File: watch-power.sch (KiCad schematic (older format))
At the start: 67 parts, among them IC1 TPS63030, IC2 MMBT2222ALT1G, IC3 BQ24230, IC4 DRV2603RUNR, IC5 LC709203F, J1 47346-0001, J2 1-1734592-4, J3 Battery, M1 Vibramotor, U1 nRF52832-QFxx, U2 APDS9960, U3 ST7735

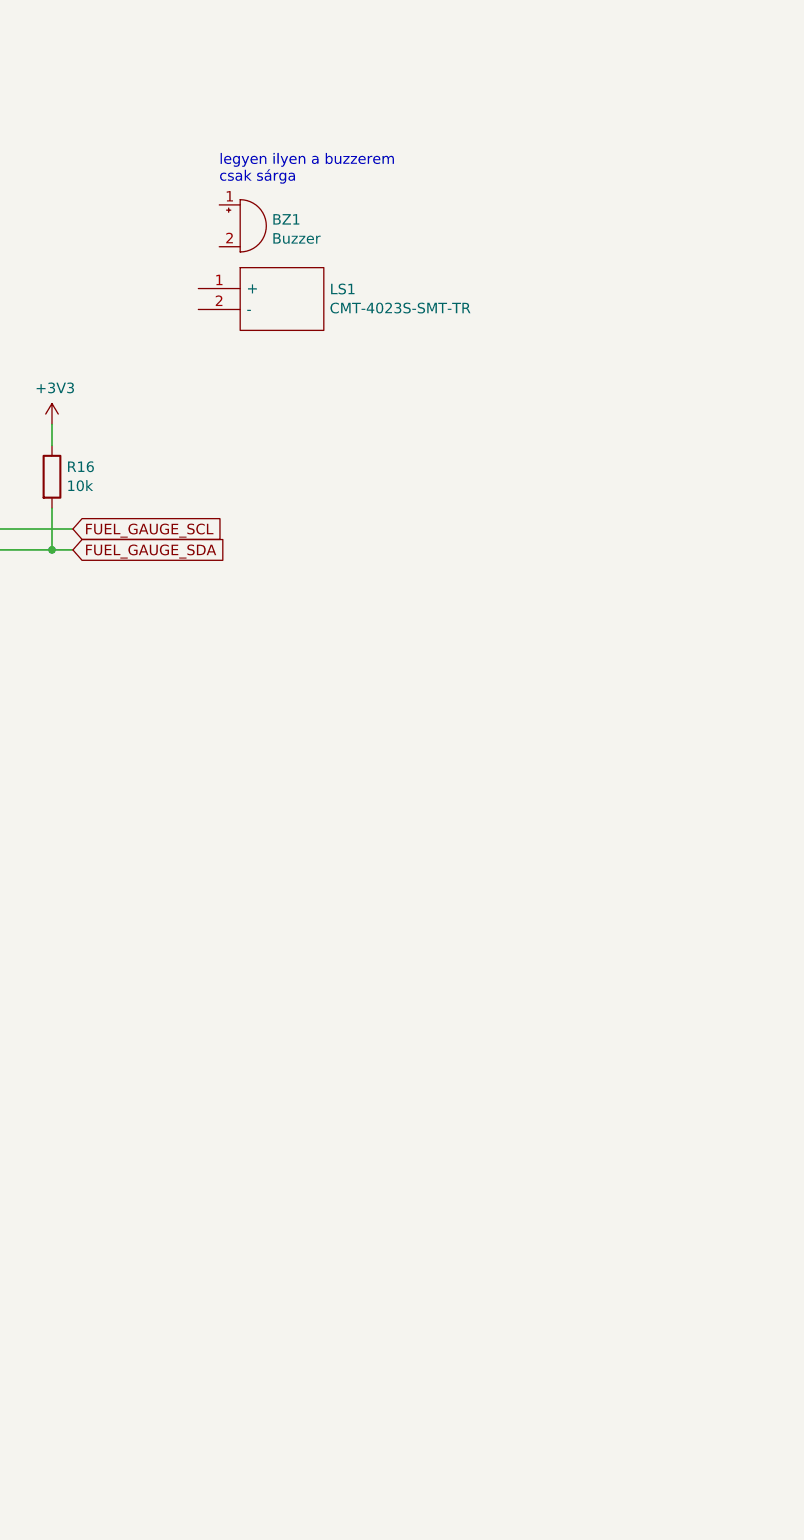
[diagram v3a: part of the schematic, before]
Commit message: add piezo
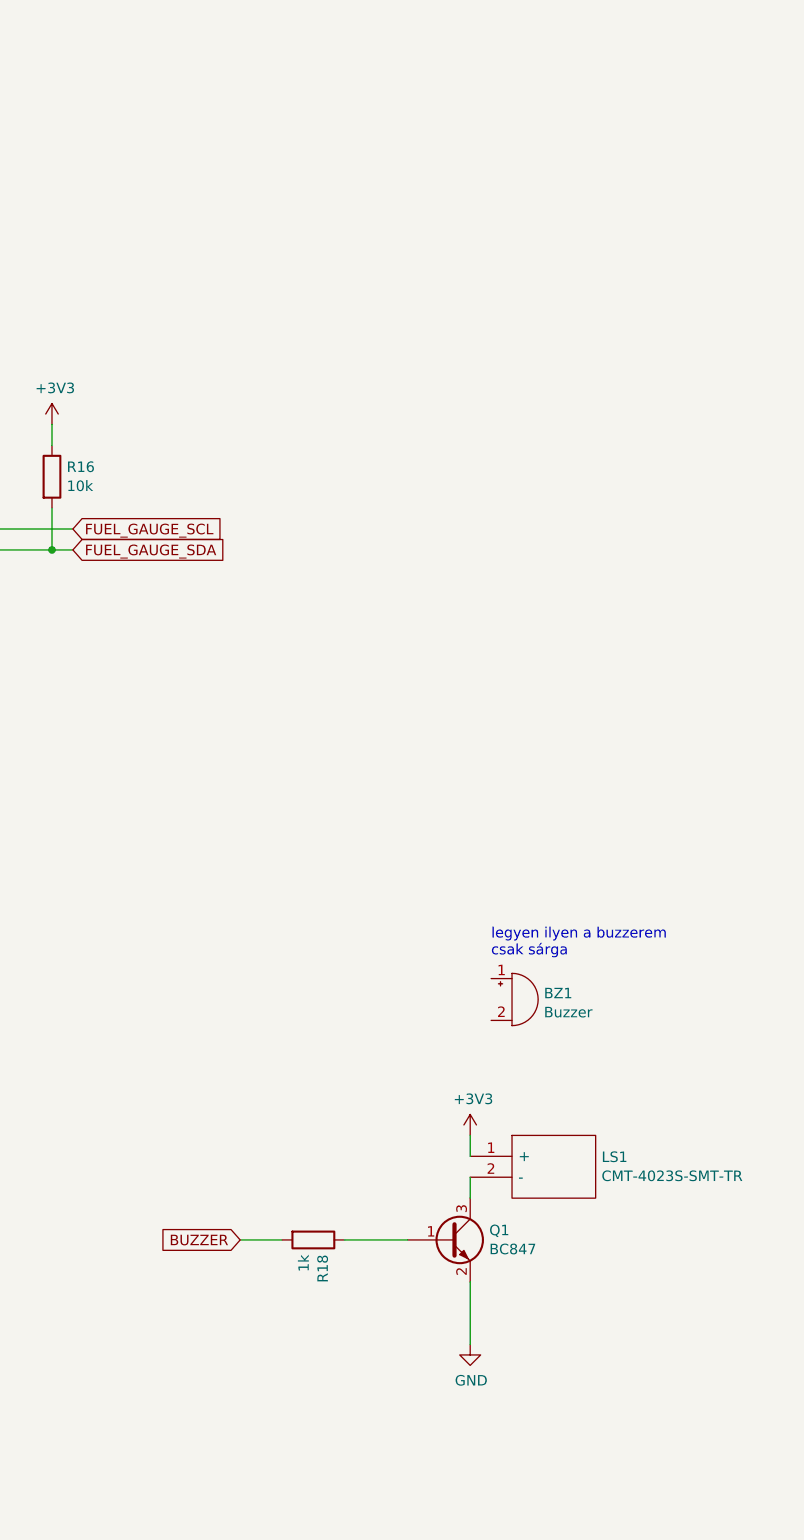
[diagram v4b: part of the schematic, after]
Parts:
- added Q1: BC847, Package_TO_SOT_SMD:SOT-23, symbol Transistor_BJT:BC847
- added R18: 1k, Resistor_SMD:R_0603_1608Metric, symbol Device:R
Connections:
- net +3V3: now also LS1.1 (+)
- net GND: now also Q1.2 (E)
- net at LS1.2 (-): now also Q1.3 (C)
- new net: Q1.1 (B), R18.1
- new net BUZZER: R18.2
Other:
- moved on the sheet: BZ1, LS1
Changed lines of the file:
@@
 L CMT-4023S-SMT-TR:CMT-4023S-SMT-TR LS1
 U 1 1 5F5A9B3D
-P 19700 5450
-F 0 "LS1" H 20328 5446 50  0000 L CNN
-F 1 "CMT-4023S-SMT-TR" H 20328 5355 50  0000 L CNN
-F 2 "CMT-4023S" H 20350 5550 50  0001 L CNN
-F 3 "http://www.cui.com/product/resource/cmt-4023s-smt.pdf" H 20350 5450 50  0001 L CNN
-F 4 "Speakers & Transducers Buzzer 4mm sq 4kHz 3V SMT" H 20350 5350 50  0001 L CNN "Description"
-F 5 "" H 20350 5250 50  0001 L CNN "Height"
-F 6 "490-CMT-4023S-SMT-TR" H 20350 5150 50  0001 L CNN "Mouser Part Number"
-F 7 "https://www.mouser.co.uk/ProductDetail/CUI-Devices/CMT-4023S-SMT-TR?qs=qCxwlXJ4fnxjBoOShJwOAQ%3D%3D" H 20350 5050 50  0001 L CNN "Mouser Price/Stock"
-F 8 "CUI Devices" H 20350 4950 50  0001 L CNN "Manufacturer_Name"
-F 9 "CMT-4023S-SMT-TR" H 20350 4850 50  0001 L CNN "Manufacturer_Part_Number"
-	1    19700 5450
+P 21000 9600
+F 0 "LS1" H 21628 9596 50  0000 L CNN
+F 1 "CMT-4023S-SMT-TR" H 21628 9505 50  0000 L CNN
+F 2 "CMT-4023S" H 21650 9700 50  0001 L CNN
+F 3 "http://www.cui.com/product/resource/cmt-4023s-smt.pdf" H 21650 9600 50  0001 L CNN
+F 4 "Speakers & Transducers Buzzer 4mm sq 4kHz 3V SMT" H 21650 9500 50  0001 L CNN "Description"
+F 5 "" H 21650 9400 50  0001 L CNN "Height"
+F 6 "490-CMT-4023S-SMT-TR" H 21650 9300 50  0001 L CNN "Mouser Part Number"
+F 7 "https://www.mouser.co.uk/ProductDetail/CUI-Devices/CMT-4023S-SMT-TR?qs=qCxwlXJ4fnxjBoOShJwOAQ%3D%3D" H 21650 9200 50  0001 L CNN "Mouser Price/Stock"
+F 8 "CUI Devices" H 21650 9100 50  0001 L CNN "Manufacturer_Name"
+F 9 "CMT-4023S-SMT-TR" H 21650 9000 50  0001 L CNN "Manufacturer_Part_Number"
+	1    21000 9600
 	1    0    0    -1
 $EndComp
@@
 L Device:Buzzer BZ1
 U 1 1 5F9D1C90
-P 19900 5150
-F 0 "BZ1" H 20052 5179 50  0000 L CNN
-F 1 "Buzzer" H 20052 5088 50  0000 L CNN
-F 2 "" V 19875 5250 50  0001 C CNN
-F 3 "~" V 19875 5250 50  0001 C CNN
-	1    19900 5150
-	1    0    0    -1
-$EndComp
-Text Notes 19800 4950 0    50   ~ 0
+P 21200 8850
+F 0 "BZ1" H 21352 8879 50  0000 L CNN
+F 1 "Buzzer" H 21352 8788 50  0000 L CNN
+F 2 "" V 21175 8950 50  0001 C CNN
+F 3 "~" V 21175 8950 50  0001 C CNN
+	1    21200 8850
+	1    0    0    -1
+$EndComp
+Text Notes 21100 8650 0    50   ~ 0
 legyen ilyen a buzzerem\ncsak sárga
 $Comp
@@
 Text Notes 14650 2350 0    50   ~ 0
 ehelyett kell a bulk storage
+$Comp
+L Transistor_BJT:BC847 Q1
+U 1 1 5F7738F3
+P 20900 10000
+F 0 "Q1" H 21091 10046 50  0000 L CNN
+F 1 "BC847" H 21091 9955 50  0000 L CNN
+F 2 "Package_TO_SOT_SMD:SOT-23" H 21100 9925 50  0001 L CIN
+F 3 "http://www.infineon.com/dgdl/Infineon-BC847SERIES_BC848SERIES_BC849SERIES_BC850SERIES-DS-v01_01-en.pdf?fileId=db3a304314dca389011541d4630a1657" H 20900 10000 50  0001 L CNN
+	1    20900 10000
+	1    0    0    -1
+$EndComp
+$Comp
+L Device:R R18
+U 1 1 5F774B1C
+P 20250 10000
+F 0 "R18" H 20320 10046 50  0000 L CNN
+F 1 "1k" H 20320 9955 50  0000 L CNN
+F 2 "Resistor_SMD:R_0603_1608Metric" V 20180 10000 50  0001 C CNN
+F 3 "~" H 20250 10000 50  0001 C CNN
+	1    20250 10000
+	0    1    1    0
+$EndComp
+Text GLabel 19900 10000 0    50   Input ~ 0
+BUZZER
+$Comp
+L power:GND #PWR0167
+U 1 1 5F77A1E3
+P 21000 10500
+F 0 "#PWR0167" H 21000 10250 50  0001 C CNN
+F 1 "GND" H 21005 10327 50  0000 C CNN
+F 2 "" H 21000 10500 50  0001 C CNN
+F 3 "" H 21000 10500 50  0001 C CNN
+	1    21000 10500
+	1    0    0    -1
+$EndComp
+$Comp
+L power:+3V3 #PWR0168
+U 1 1 5F77BCBE
+P 21000 9500
+F 0 "#PWR0168" H 21000 9350 50  0001 C CNN
+F 1 "+3V3" H 21015 9673 50  0000 C CNN
+F 2 "" H 21000 9500 50  0001 C CNN
+F 3 "" H 21000 9500 50  0001 C CNN
+	1    21000 9500
+	1    0    0    -1
+$EndComp
+Wire Wire Line
+	21000 9600 21000 9500
+Wire Wire Line
+	21000 9700 21000 9800
+Wire Wire Line
+	21000 10200 21000 10500
+Wire Wire Line
+	20700 10000 20400 10000
+Wire Wire Line
+	19900 10000 20100 10000
 $EndSCHEMATC

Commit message: save before drastic rearranger
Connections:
- net +3V3: now also C26.1
- net GND: now also C26.2
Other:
- moved on the sheet: C26
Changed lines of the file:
@@
 Text Notes 10300 1250 0    50   ~ 0
 BATTERY vagy 3v3?
-Text Notes 16850 1150 0    50   ~ 0
+Text Notes 19300 700  0    50   ~ 0
 legyen szélesebb a szimbólum\n
 Text GLabel 9850 3950 0    50   Input ~ 0
@@
 L Device:C C26
 U 1 1 5F730623
-P 15150 2200
-F 0 "C26" H 15265 2246 50  0000 L CNN
-F 1 "10uF" H 15265 2155 50  0000 L CNN
-F 2 "" H 15188 2050 50  0001 C CNN
-F 3 "~" H 15150 2200 50  0001 C CNN
-	1    15150 2200
+P 15500 2250
+F 0 "C26" H 15615 2296 50  0000 L CNN
+F 1 "10uF" H 15615 2205 50  0000 L CNN
+F 2 "" H 15538 2100 50  0001 C CNN
+F 3 "~" H 15500 2250 50  0001 C CNN
+	1    15500 2250
 	1    0    0    -1
 $EndComp
@@
 Wire Wire Line
 	17500 10000 17500 9900
-Text Notes 14650 2350 0    50   ~ 0
+Text Notes 19200 3900 0    50   ~ 0
 ehelyett kell a bulk storage
 $Comp
